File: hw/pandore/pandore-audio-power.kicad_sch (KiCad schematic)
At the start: 76 parts, among them J22 V12ISO, J23 AV5, J24 AV3P3, Q7 MOSFET_EN-N, U12 NXES2, U13 LDL212DR, U14 LDL212DR, U21 LM5158, U22 TPS7A4001

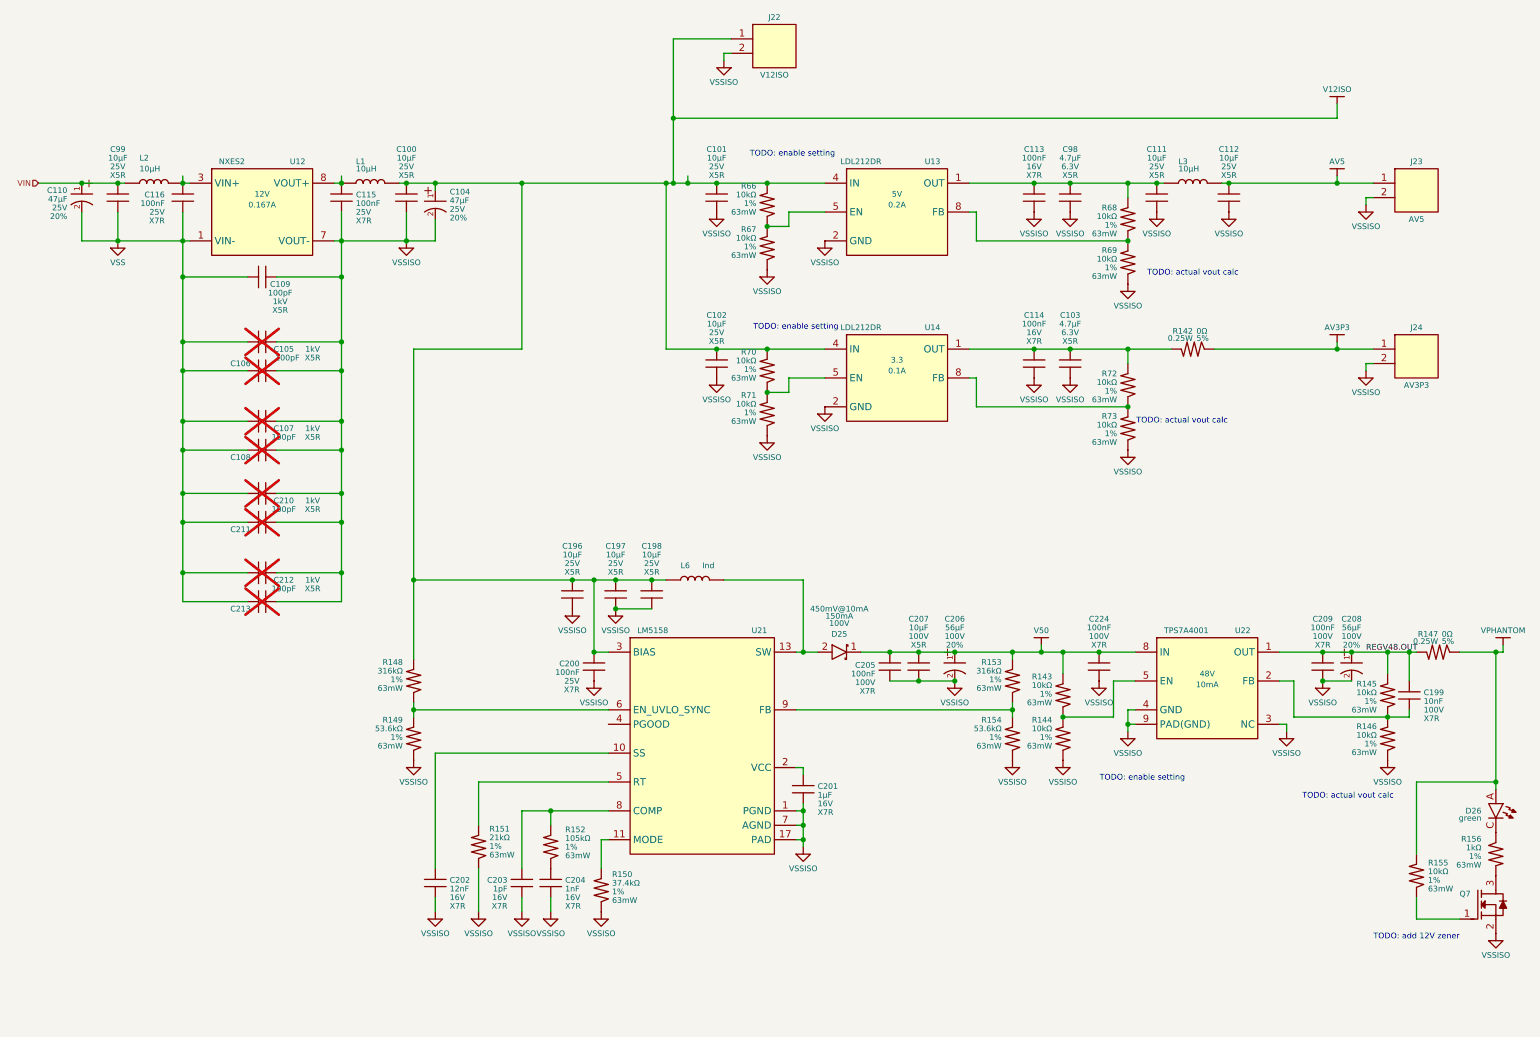
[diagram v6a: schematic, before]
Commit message: most of board control signals added, routed and defined
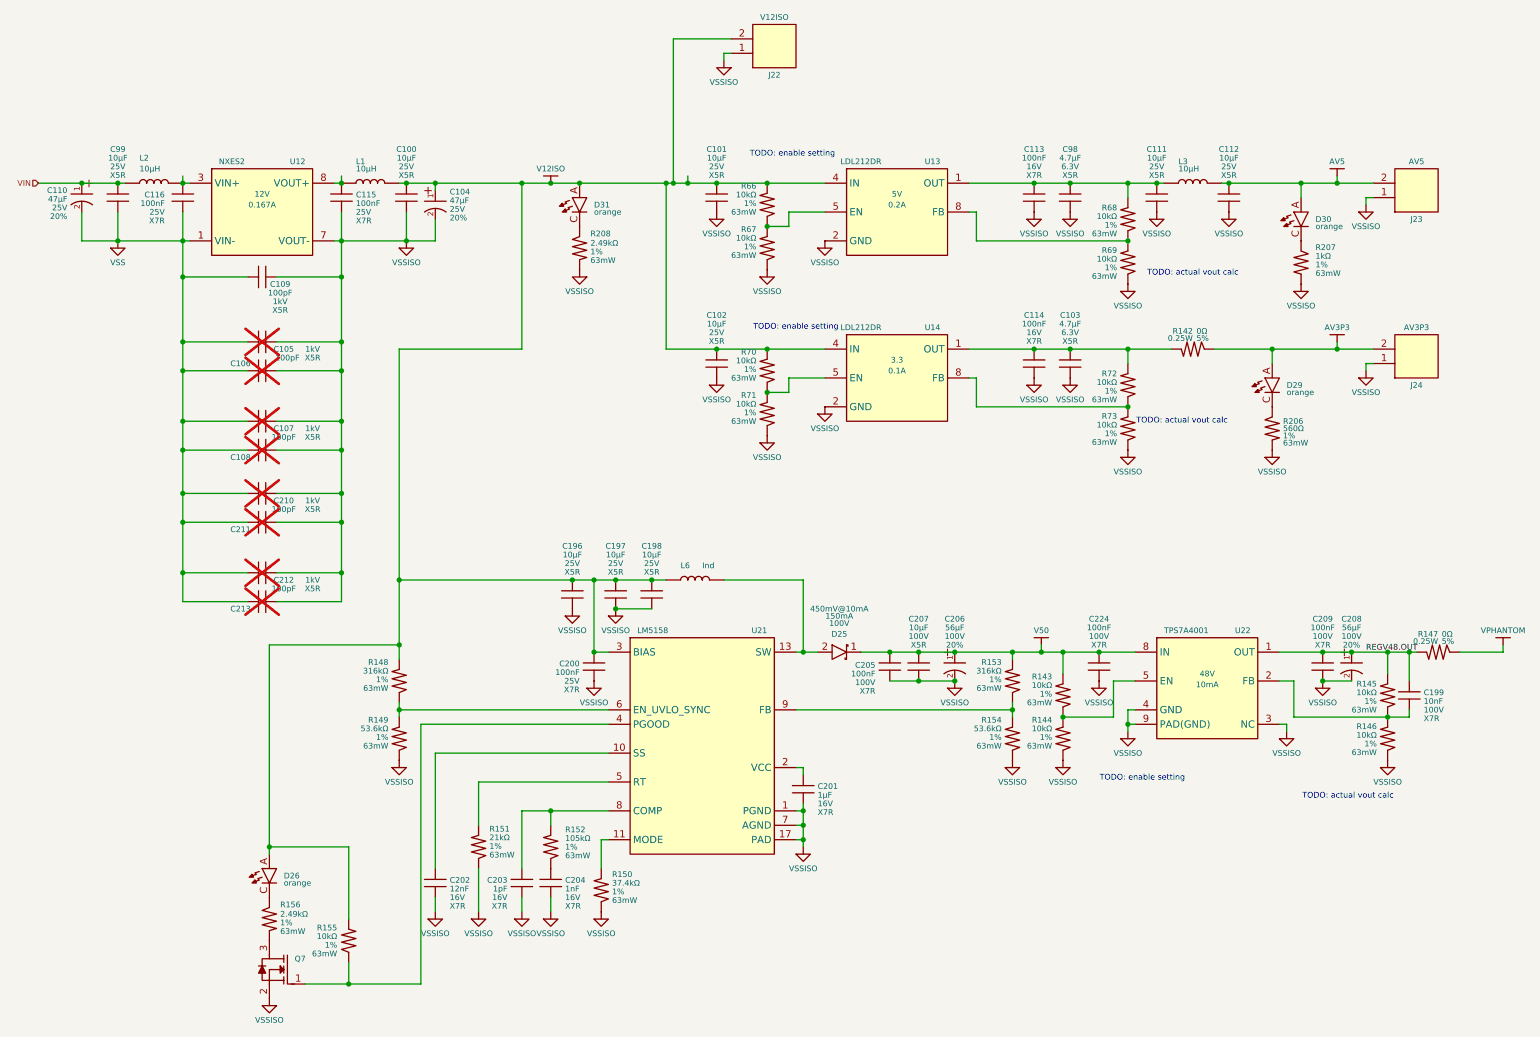
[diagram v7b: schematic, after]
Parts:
- added D29, D30, D31: ${color}, reekilib_led:LEDM1608X80, symbol reekilib_led:led
- added R206, R207, R208: ${Resistance}, ${Tolerance}, ${Power}, reekilib_res:RESC1005, symbol reekilib_res:res
- D26: Link https://ams-osram.com/products/leds/color-leds/osram-smartled-0603-kt-eelp41-12 -> https://ams-osram.com/products/leds/color-leds/osram-smartled-0603-ko-eelp41-22; Vf 2.5V -> 2.0V; Vr 1.2V -> 10V; color green -> orange; lum 224mcd@5mA -> 392mcd@5mA; λdom 527nm -> 610nm
- J22, J23: footprint reekilib_con:Wurth_691137710002 -> reekilib_con:HDR254P1X02-TH; Link https://www.we-online.com/en/components/products/TBL_5_00_1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 -> (none); MFG Wurth -> (none); MPN 691137710002 -> (none)
- J24: footprint reekilib_con:Wurth_691137710002 -> reekilib_con:HDR254P1X02-TH; MFG Wurth -> (none); MPN 691137710002 -> (none)
- R156: Resistance 1kΩ -> 2.49kΩ
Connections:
- net AV3P3: now also J24.2, D29.A; no longer J24.1
- net AV5: now also J23.2, D30.A; no longer J23.1
- net V12ISO: now also D26.A, J22.2, R155.1, D31.A; no longer J22.1
- net VPHANTOM: no longer D26.A, R155.1
- net VSSISO: now also J22.1, J23.1, J24.1, R206.1, R207.1, R208.1; no longer J22.2, J23.2, J24.2
- net at Q7.1 (G), R155.2: now also U21.4 (PGOOD)
- new net: D30.C, R207.2
- new net: D31.C, R208.2
- new net: D29.C, R206.2
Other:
- note removed: "TODO: add 12V zener"
- moved on the sheet: Q7, R148, R149, R155
